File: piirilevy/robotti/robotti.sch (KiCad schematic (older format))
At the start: 41 parts

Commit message: korjattu lämpömittari
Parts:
- removed C?: C, symbol Device:C
- removed R?: R, symbol Device:R
- added C?: 1uF, symbol Device:C
- C?: value C -> 680pF
- C?: value C -> 0.1uF
- R?: value R -> 10K
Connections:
- net GND: now also C?.2, R?.2; no longer C?.1
- net VDD: now also C?.2; no longer Q?.1 (C)
- net at U?.15 (PA1): now also C?.1, U?.2 (Vout)
- new net: C?.1, Q?.1 (C)
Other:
- moved on the sheet: C?, R?, U?
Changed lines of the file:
@@
 U 1 1 60648B84
 P 4600 2350
-F 0 "C?" V 4450 2350 50  0000 C CNN
-F 1 "0.1uF" V 4350 2350 50  0000 C CNN
+F 0 "C?" H 4350 2400 50  0000 C CNN
+F 1 "0.1uF" H 4350 2300 50  0000 C CNN
 F 2 "" H 4638 2200 50  0001 C CNN
 F 3 "~" H 4600 2350 50  0001 C CNN
@@
 L robotti_library:TMP235 U?
 U 1 1 6079B556
-P 7500 2600
-F 0 "U?" H 7170 2554 50  0000 R CNN
-F 1 "TMP235" H 7170 2645 50  0000 R CNN
-F 2 "Package_TO_SOT_SMD:SOT-323_SC-70" H 7500 2200 50  0001 C CNN
-F 3 "http://www.ti.com/lit/ds/symlink/tmp20.pdf" H 7500 2600 50  0001 C CNN
-	1    7500 2600
+P 7500 2900
+F 0 "U?" H 7170 2854 50  0000 R CNN
+F 1 "TMP235" H 7170 2945 50  0000 R CNN
+F 2 "Package_TO_SOT_SMD:SOT-323_SC-70" H 7500 2500 50  0001 C CNN
+F 3 "http://www.ti.com/lit/ds/symlink/tmp20.pdf" H 7500 2900 50  0001 C CNN
+	1    7500 2900
 	-1   0    0    1
-$EndComp
-$Comp
-L Device:R R?
-U 1 1 607A94D2
-P 6850 2400
-F 0 "R?" V 6950 2400 50  0000 C CNN
-F 1 "R" V 7050 2400 50  0000 C CNN
-F 2 "" V 6780 2400 50  0001 C CNN
-F 3 "~" H 6850 2400 50  0001 C CNN
-	1    6850 2400
-	0    1    1    0
 $EndComp
 $Comp
 L Device:C C?
 U 1 1 607AA380
-P 7300 2100
-F 0 "C?" V 7550 2100 50  0000 C CNN
-F 1 "C" V 7450 2100 50  0000 C CNN
-F 2 "" H 7338 1950 50  0001 C CNN
-F 3 "~" H 7300 2100 50  0001 C CNN
-	1    7300 2100
-	0    1    1    0
+P 7250 2400
+F 0 "C?" V 7500 2400 50  0000 C CNN
+F 1 "680pF" V 7400 2400 50  0000 C CNN
+F 2 "" H 7288 2250 50  0001 C CNN
+F 3 "~" H 7250 2400 50  0001 C CNN
+	1    7250 2400
+	0    -1   -1   0
 $EndComp
 $Comp
 L power:GND #PWR?
 U 1 1 607BA8CF
-P 7850 2100
-F 0 "#PWR?" H 7850 1850 50  0001 C CNN
-F 1 "GND" V 7750 2000 50  0000 R CNN
-F 2 "" H 7850 2100 50  0001 C CNN
-F 3 "" H 7850 2100 50  0001 C CNN
-	1    7850 2100
+P 7800 2400
+F 0 "#PWR?" H 7800 2150 50  0001 C CNN
+F 1 "GND" V 7700 2300 50  0000 R CNN
+F 2 "" H 7800 2400 50  0001 C CNN
+F 3 "" H 7800 2400 50  0001 C CNN
+	1    7800 2400
 	0    -1   -1   0
 $EndComp
@@
 L power:VDD #PWR?
 U 1 1 607C0535
-P 7500 3100
-F 0 "#PWR?" H 7500 2950 50  0001 C CNN
-F 1 "VDD" V 7515 3227 50  0000 L CNN
-F 2 "" H 7500 3100 50  0001 C CNN
-F 3 "" H 7500 3100 50  0001 C CNN
-	1    7500 3100
+P 7500 3400
+F 0 "#PWR?" H 7500 3250 50  0001 C CNN
+F 1 "VDD" H 7550 3500 50  0000 L CNN
+F 2 "" H 7500 3400 50  0001 C CNN
+F 3 "" H 7500 3400 50  0001 C CNN
+	1    7500 3400
 	-1   0    0    1
 $EndComp
@@
 L Device:C C?
 U 1 1 607C1C96
-P 7700 3000
-F 0 "C?" V 7950 3000 50  0000 C CNN
-F 1 "C" V 7850 3000 50  0000 C CNN
-F 2 "" H 7738 2850 50  0001 C CNN
-F 3 "~" H 7700 3000 50  0001 C CNN
-	1    7700 3000
-	0    1    1    0
-$EndComp
-Wire Wire Line
-	7500 2900 7500 3000
-Wire Wire Line
-	7550 3000 7500 3000
-Connection ~ 7500 3000
-Wire Wire Line
-	7500 3000 7500 3100
+P 7700 3300
+F 0 "C?" V 7950 3300 50  0000 C CNN
+F 1 "0.1uF" V 7850 3300 50  0000 C CNN
+F 2 "" H 7738 3150 50  0001 C CNN
+F 3 "~" H 7700 3300 50  0001 C CNN
+	1    7700 3300
+	0    1    1    0
+$EndComp
+Wire Wire Line
+	7500 3200 7500 3300
+Wire Wire Line
+	7550 3300 7500 3300
+Connection ~ 7500 3300
+Wire Wire Line
+	7500 3300 7500 3400
 $Comp
 L power:GND #PWR?
 U 1 1 607CC73F
-P 7850 3000
-F 0 "#PWR?" H 7850 2750 50  0001 C CNN
-F 1 "GND" V 7950 2950 50  0000 R CNN
-F 2 "" H 7850 3000 50  0001 C CNN
-F 3 "" H 7850 3000 50  0001 C CNN
-	1    7850 3000
-	0    -1   -1   0
-$EndComp
-Wire Wire Line
-	7500 2100 7500 2300
-Wire Wire Line
-	7100 2100 7100 2400
-Wire Wire Line
-	6450 2400 6700 2400
+P 7850 3300
+F 0 "#PWR?" H 7850 3050 50  0001 C CNN
+F 1 "GND" V 7950 3250 50  0000 R CNN
+F 2 "" H 7850 3300 50  0001 C CNN
+F 3 "" H 7850 3300 50  0001 C CNN
+	1    7850 3300
+	0    -1   -1   0
+$EndComp
+Wire Wire Line
+	7500 2400 7500 2600
 Wire Wire Line
 	8000 1600 7750 1600
@@
 $EndComp
 Wire Wire Line
-	7000 2400 7100 2400
-Connection ~ 7100 2400
-Wire Wire Line
-	7100 2400 7100 2600
-Wire Wire Line
 	4400 3500 4650 3500
 Wire Wire Line
@@
 L Device:R R?
 U 1 1 6083078D
-P 6900 2100
-F 0 "R?" V 6800 2100 50  0000 C CNN
-F 1 "R" V 6700 2100 50  0000 C CNN
-F 2 "" V 6830 2100 50  0001 C CNN
-F 3 "~" H 6900 2100 50  0001 C CNN
-	1    6900 2100
-	0    -1   -1   0
-$EndComp
-Connection ~ 7100 2100
+P 6900 1800
+F 0 "R?" V 6800 1800 50  0000 C CNN
+F 1 "10K" V 6700 1800 50  0000 C CNN
+F 2 "" V 6830 1800 50  0001 C CNN
+F 3 "~" H 6900 1800 50  0001 C CNN
+	1    6900 1800
+	0    -1   -1   0
+$EndComp
+Wire Wire Line
+	6700 2300 6450 2300
+Wire Wire Line
+	7050 1800 7100 1800
+Wire Wire Line
+	6700 1200 6700 1350
+Wire Wire Line
+	7550 1150 7550 1200
+$Comp
+L power:GND #PWR?
+U 1 1 6065F0ED
+P 7100 1800
+F 0 "#PWR?" H 7100 1550 50  0001 C CNN
+F 1 "GND" V 7200 1800 50  0000 R CNN
+F 2 "" H 7100 1800 50  0001 C CNN
+F 3 "" H 7100 1800 50  0001 C CNN
+	1    7100 1800
+	0    -1   -1   0
+$EndComp
 $Comp
 L Device:C C?
-U 1 1 60831578
-P 6900 1900
-F 0 "C?" V 7150 1900 50  0000 C CNN
-F 1 "C" V 7050 1900 50  0000 C CNN
-F 2 "" H 6938 1750 50  0001 C CNN
-F 3 "~" H 6900 1900 50  0001 C CNN
-	1    6900 1900
-	0    -1   -1   0
-$EndComp
-Wire Wire Line
-	6700 2300 6450 2300
-Wire Wire Line
-	7100 1900 7100 2100
-Wire Wire Line
-	7050 2100 7100 2100
-Wire Wire Line
-	7050 1900 7100 1900
-Wire Wire Line
-	6700 1750 6700 1900
-Wire Wire Line
-	6750 1900 6700 1900
-Connection ~ 6700 1900
-Wire Wire Line
-	6700 1900 6700 2100
-Wire Wire Line
-	6750 2100 6700 2100
-Connection ~ 6700 2100
-Wire Wire Line
-	6700 2100 6700 2300
-Wire Wire Line
-	7550 1200 6700 1200
-Wire Wire Line
-	6700 1200 6700 1350
-Wire Wire Line
-	7550 1150 7550 1200
-Wire Wire Line
-	7500 2100 7850 2100
-Wire Wire Line
-	7450 2100 7500 2100
-Connection ~ 7500 2100
-Wire Wire Line
-	7150 2100 7100 2100
+U 1 1 606750D5
+P 7000 1200
+F 0 "C?" V 7250 1200 50  0000 C CNN
+F 1 "1uF" V 7150 1200 50  0000 C CNN
+F 2 "" H 7038 1050 50  0001 C CNN
+F 3 "~" H 7000 1200 50  0001 C CNN
+	1    7000 1200
+	0    -1   -1   0
+$EndComp
+Wire Wire Line
+	7150 1200 7550 1200
+Wire Wire Line
+	6850 1200 6700 1200
+Wire Wire Line
+	6700 1750 6700 1800
+Wire Wire Line
+	6750 1800 6700 1800
+Connection ~ 6700 1800
+Wire Wire Line
+	6700 1800 6700 2300
+Wire Wire Line
+	7500 2400 7800 2400
+Connection ~ 7500 2400
+Wire Wire Line
+	6950 2900 7100 2900
+Wire Wire Line
+	6450 2400 6950 2400
+Wire Wire Line
+	7400 2400 7500 2400
+Wire Wire Line
+	7100 2400 6950 2400
+Connection ~ 6950 2400
+Wire Wire Line
+	6950 2400 6950 2900
 $EndSCHEMATC

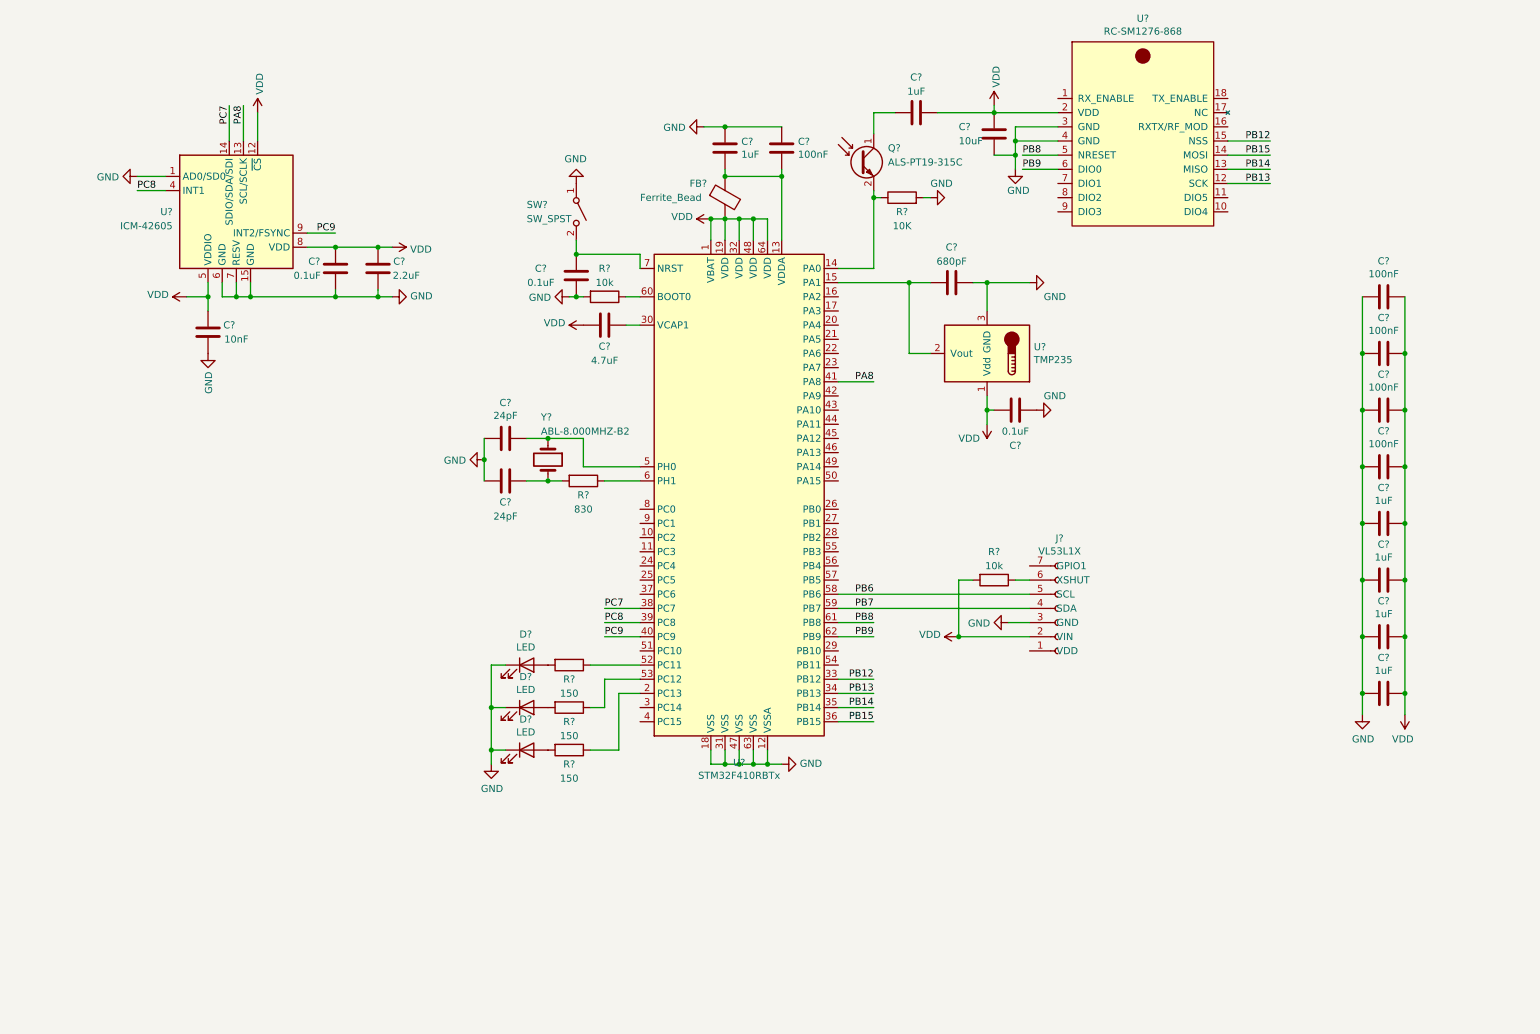
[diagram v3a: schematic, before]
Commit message: lisätty toinen etäisyyssensori + annotointi symboleille
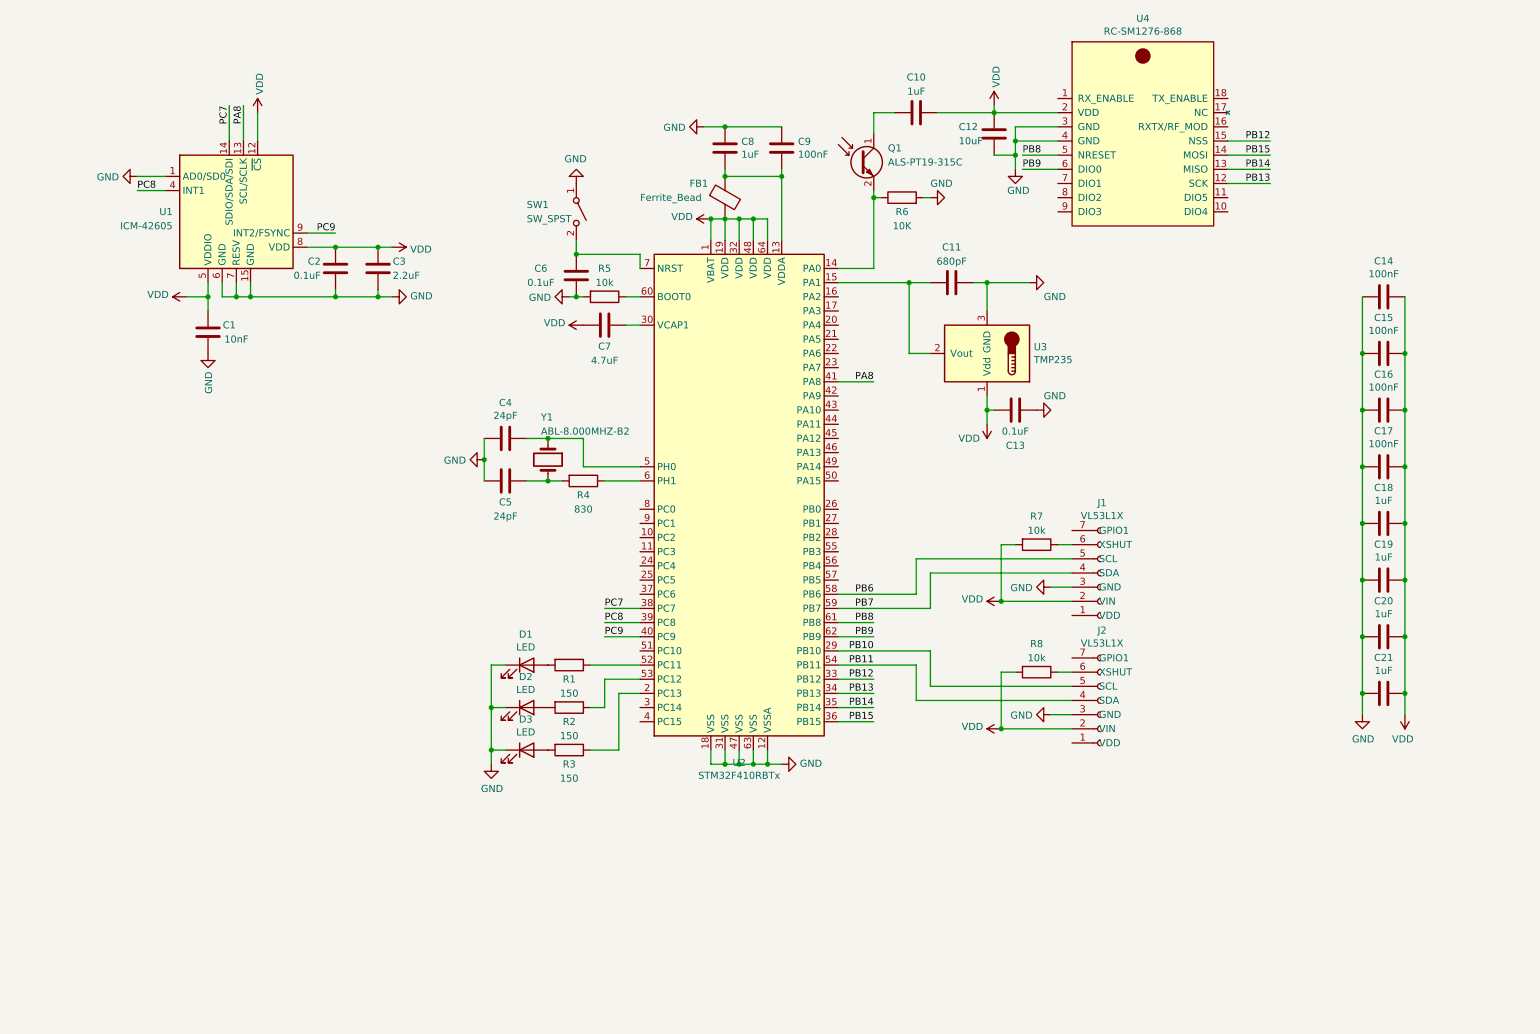
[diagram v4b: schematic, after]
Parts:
- added J2: VL53L1X, Connector_JST:JST_XH_B7B-XH-AM_1x07_P2.50mm_Vertical, symbol robotti_library:VL53L1X
- added R8: 10k, symbol Device:R
- gave numbers to parts that had none: 40
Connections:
- net GND: now also J2.3 (GND)
- net VDD: now also J2.2 (VIN), R8.2
- net PB10: now reaches U2.29 (PB10)
- net PB10: now also J2.5 (SCL)
- net PB11: now reaches U2.54 (PB11)
- net PB11: now also J2.4 (SDA)
- new net: J2.6 (XSHUT), R8.1
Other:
- moved on the sheet: J1, R7

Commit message: Regulointi lisätty
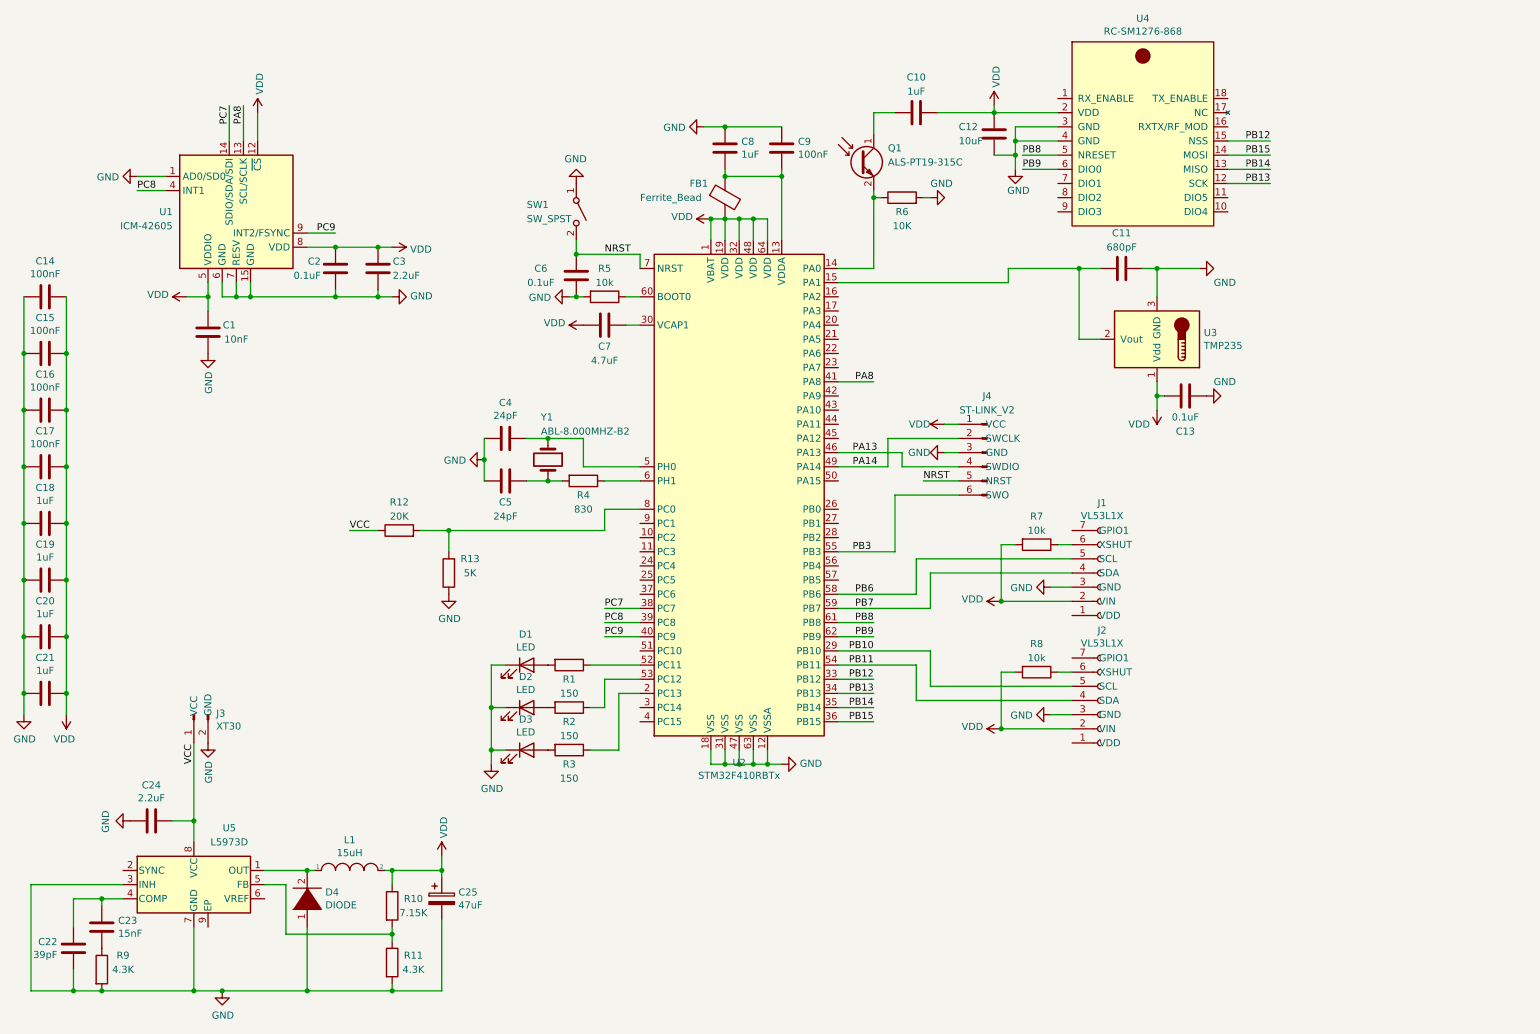
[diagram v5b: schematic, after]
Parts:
- added C22: 39pF, symbol Device:C
- added C23: 15nF, symbol Device:C
- added C24: 2.2uF, Capacitor_SMD:C_0805_2012Metric, symbol Device:C
- added C25: 47uF, symbol Device:CP
- added D4: DIODE, symbol pspice:DIODE
- added J3: XT30, Connector_AMASS:AMASS_XT30U-F_1x02_P5.0mm_Vertical, symbol robotti_library:XT30
- added J4: ST-LINK_V2, Connector_PinHeader_2.54mm:PinHeader_1x06_P2.54mm_Vertical, symbol robotti_library:ST-LINK_V2
- added L1: 15uH, Inductor_SMD:L_Bourns_SRR1260, symbol pspice:INDUCTOR
- added R10: 7.15K, symbol Device:R
- added R11, R9: 4.3K, symbol Device:R
- added R12: 20K, symbol Device:R
- added R13: 5K, symbol Device:R
- added U5: L5973D, Package_SO:HSOP-8-1EP_3.9x4.9mm_P1.27mm_EP2.41x3.1mm_ThermalVias, symbol Regulator_Switching:L5973D
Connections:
- net GND: now also C22.1, C24.1, C25.2, D4.1 (K), J3.2 (GND), J4.3 (GND), R11.2, R13.1, R9.2, U5.3 (INH), U5.7 (GND)
- net VDD: now also C25.1, J4.1 (VCC), L1.2, R10.1
- net PA13: now reaches U2.46 (PA13)
- net PA13: now also J4.4 (SWDIO)
- net PA14: now reaches U2.49 (PA14)
- net PA14: now also J4.2 (SWCLK)
- net PB3: now reaches U2.55 (PB3)
- net PB3: now also J4.6 (SWO)
- net NRST: now reaches C6.1, SW1.2 (B), U2.7 (NRST)
- net NRST: now also J4.5 (NRST)
- net at U2.8 (PC0): now also R12.2, R13.2
- new net: D4.2 (A), L1.1, U5.1 (OUT)
- new net: C22.2, C23.2, U5.4 (COMP)
- new net: R10.2, R11.1, U5.5 (FB)
- new net: C23.1, R9.1
- new net VCC: C24.2, J3.1 (VCC), R12.1, U5.8 (VCC)
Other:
- moved on the sheet: C11, C13, C14, C15, C16, C17, C18, C19, C20, C21, U3

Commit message: Schema valmis + aloitettu pcb
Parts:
- added C26, C27: 100uF, Capacitor_SMD:CP_Elec_8x5.4, symbol Device:CP
- added J5: UART, Connector_PinHeader_2.54mm:PinHeader_1x03_P2.54mm_Vertical, symbol robotti_library:UART
- added J6, J7: Nema14, Connector_JST:JST_PH_B4B-PH-K_1x04_P2.00mm_Vertical, symbol robotti_library:Nema14
- added JP1, JP2: TMC2130-Connector_JP, robotti:TMC2130, symbol robotti_library:TMC2130-Connector_JP
- C1, C10, C11, C12, C13, C14, C15, C16, C17, C18, C19, C2, C20, C21, C22, C23, C3, C4, C5, C6, C7, C8, C9: footprint (none) -> Capacitor_SMD:C_0805_2012Metric
- C25: footprint (none) -> Capacitor_SMD:CP_Elec_6.3x5.4_Nichicon
- D1, D2, D3: footprint (none) -> LED_SMD:LED_0805_2012Metric
- D4: footprint (none) -> Diode_SMD:D_SMB
- FB1, R1, R10, R11, R12, R13, R2, R3, R4, R5, R6, R7, R8, R9: footprint (none) -> Resistor_SMD:R_0805_2012Metric
- J1, J2: footprint Connector_JST:JST_XH_B7B-XH-AM_1x07_P2.50mm_Vertical -> Connector_JST:JST_SH_BM07B-SRSS-TB_1x07-1MP_P1.00mm_Vertical
- SW1: footprint (none) -> Button_Switch_SMD:SW_SPST_TL3305A
- U4: footprint (none) -> robotti:RC-SM1276-868
- Y1: footprint (none) -> Crystal:Crystal_HC49-U_Vertical
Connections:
- net GND: now also C26.2, C27.2, J5.3 (GND), JP1.10 (GND), JP1.16 (GND), JP2.10 (GND), JP2.16 (GND)
- net VCC: now also C26.1, C27.1, JP1.9 (VM), JP2.9 (VM)
- net VDD: now also JP1.15 (VIO), JP2.15 (VIO)
- net PC2: now reaches U2.10 (PC2)
- net PC2: now also JP1.2 (STEP)
- net PC3: now reaches U2.11 (PC3)
- net PC3: now also JP1.8 (En/CFG6)
- net VDDA: now reaches C8.2, C9.2, FB1.1, U2.13 (VDDA)
- net PA2: now reaches U2.16 (PA2)
- net PA2: now also J5.1 (TX)
- net PA3: now reaches U2.17 (PA3)
- net PA3: now also J5.2 (RX)
- net PA4: now reaches U2.20 (PA4)
- net PA4: now also JP1.5 (CS/CFG3)
- net PA5: now reaches U2.21 (PA5)
- net PA5: now also JP1.6 (SCK/CFG2)
- net PA6: now reaches U2.22 (PA6)
- net PA6: now also JP1.4 (SDO/CFG0)
- net PA7: now reaches U2.23 (PA7)
- net PA7: now also JP1.7 (SDI/CFG1)
- net PC4: now reaches U2.24 (PC4)
- net PC4: now also JP2.1 (DIR)
- net PC5: now reaches U2.25 (PC5)
- net PC5: now also JP2.2 (STEP)
- net PB0: now reaches U2.26 (PB0)
- net PB0: now also JP2.6 (SCK/CFG2)
- net PB1: now reaches U2.27 (PB1)
- net PB1: now also JP2.5 (CS/CFG3)
- net PA9: now reaches U2.42 (PA9)
- net PA9: now also JP2.8 (En/CFG6)
- net PA10: now reaches U2.43 (PA10)
- net PA10: now also JP2.7 (SDI/CFG1)
- net PA12: now reaches U2.45 (PA12)
- net PA12: now also JP2.4 (SDO/CFG0)
- net PC0: now reaches R12.2, R13.2, U2.8 (PC0)
- net PC1: now reaches U2.9 (PC1)
- net PC1: now also JP1.1 (DIR)
- new net: J7.4 (B2), JP2.11 (OB2)
- new net: J7.3 (B1), JP2.12 (OB1)
- new net: J7.2 (A2), JP2.13 (OA1)
- new net: J7.1 (A1), JP2.14 (OA2)
- new net: J6.4 (B2), JP1.11 (OB2)
- new net: J6.3 (B1), JP1.12 (OB1)
- new net: J6.2 (A2), JP1.13 (OA1)
- new net: J6.1 (A1), JP1.14 (OA2)
- no-connect marks 0 -> 24
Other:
- note added: "Debug-liitin (UART)"
- note added: "Etäisyyssensori 1"
- note added: "Etäisyyssensori 2"
- note added: "Jännitemittaus akusta"
- note added: "Kiihtyvyyssensori IMU"
- note added: "LoRa-radio"
- note added: "Lämpötilasensori"
- note added: "Nema14 liitin"
- note added: "Ohjelmointiliitin"
- note added: "Regulaattori 3,3 V"
- note added: "Stepper-ohjain 1"
- note added: "Stepper-ohjain 2"
- note added: "Valoisuusanturi"
- note added: "Virransyöttö akusta 11,1 - 14 V"
